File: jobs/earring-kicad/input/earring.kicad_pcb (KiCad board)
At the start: 4 copper layers, 30.5 x 35.8 mm, 144 parts, among them J1 USB-C, Q1 ALS-PT19, Q2 CJ2101, Q3 BSS138W, Q4 CJ2101, Q5 BSS138W, SW1 BOOTSEL, SW2 PWR, U1 RP2350A, U2 LGS4056H, U3 NCP730-3.3, U4 TPS22913, U5 USBLC6-2P6, U6 LSM6DS3TR-C, U7 W25Q16JVUXIQ, Y1 12MHz

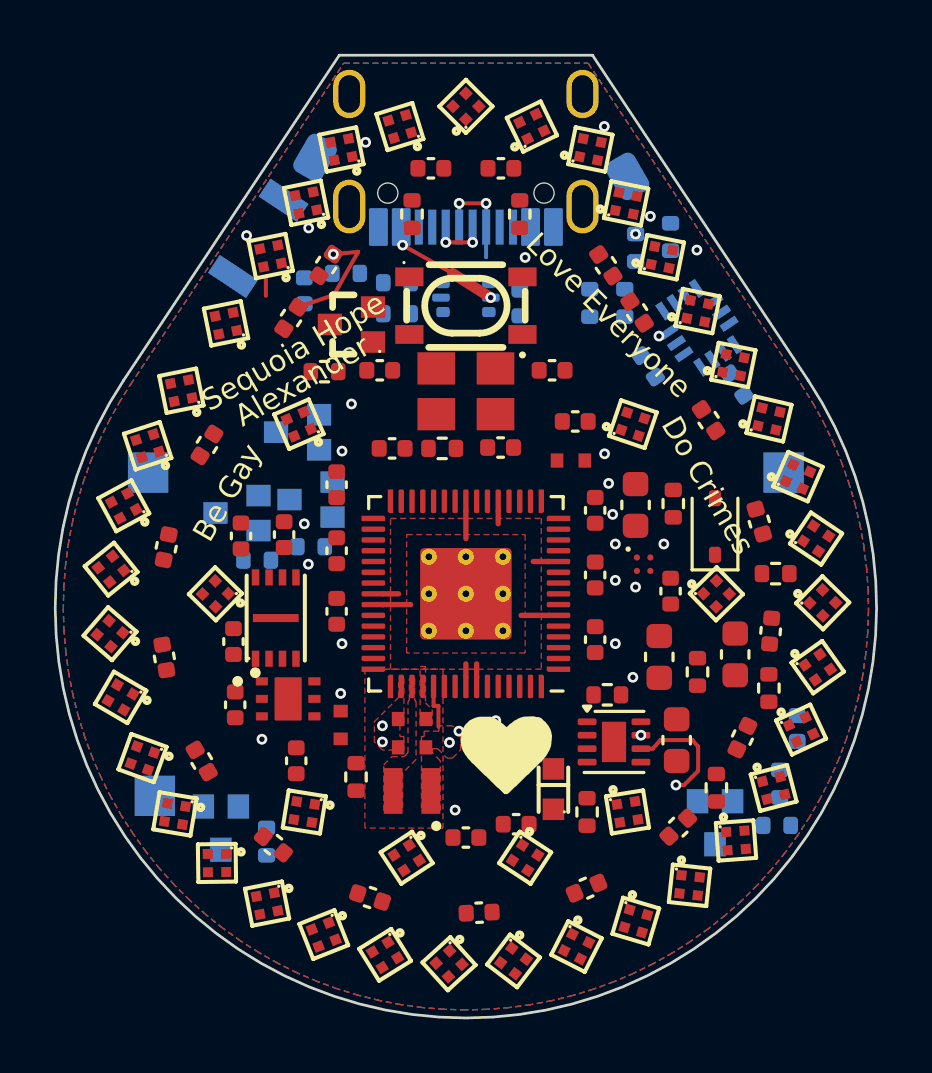
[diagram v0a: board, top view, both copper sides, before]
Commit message: Studio: KiCad colours and controls, views by side, router activity, fading congestion; the latest earring
The studio offers only the KiCad boards marked for it, bluebuzz and the earring, both from bare
pads (--strip-all), and the earring is now simple-earring's latest board (78920f1, the WS2816C
ring). It draws in KiCad's default colours with an active layer, high contrast and a flipped
view, takes KiCad's view keys, and shows all layers, the top, the bottom or both side by side.
The router reports what it is doing: a console streams its activity, the connection or part in
hand pulses on the board, and negotiation's threaded rounds show their trial routes as they come.
Congestion cells pop in when they change and fade while they stay. Old zone fills are hidden by
default, hovering a lock highlights its parts, and Route says what a run will do, with moving
parts a switch rather than a second button.

Co-Authored-By: Claude Opus 5.5 <noreply@anthropic.com>
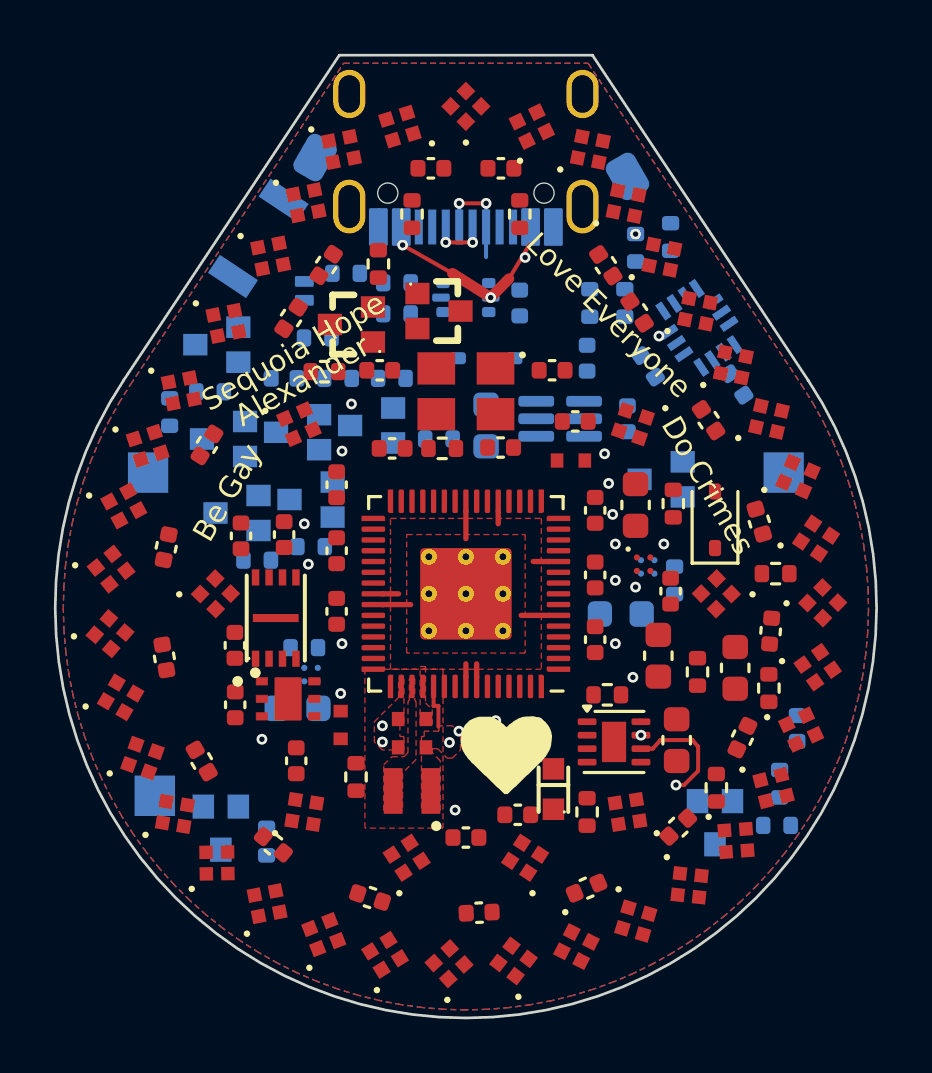
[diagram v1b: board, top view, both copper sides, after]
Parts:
- removed SW1: BOOTSEL, earring:KEY-SMD_4P-L4.2-W3.2-P2.20-LS4.6
- added C75: 10u, earring:C_0603_1608Metric, B.Cu at (100.8, 93.2)
- added C76: 10n, earring:C_0402_1005Metric, B.Cu at (104.5, 90.8)
- added C77: 100n, earring:C_0402_1005Metric, B.Cu at (106.0, 93.0)
- added C78: 10u, earring:C_0603_1608Metric, B.Cu at (105.8, 100.2)
- added C79: 10u, earring:C_0603_1608Metric, B.Cu at (93.8, 103.8)
- added D5: 1N4148WS, earring:D_SOD-323, B.Cu at (100.8, 90.8)
- added D6: PESD5V0S1BL, earring:D_SOD-882, B.Cu at (94.0, 88.2)
- added Q10: BSS138W, earring:SOT-323_MOSFET, B.Cu at (91.0, 93.8)
- added Q6: BSS138W, earring:SOT-323_MOSFET, F.Cu at (99.0, 89.0)
- added Q7: BSS138W, earring:SOT-323_MOSFET, B.Cu at (107.2, 95.2)
- added Q8: CJ2101, earring:SOT-323_MOSFET, B.Cu at (96.5, 93.2)
- added Q9: BSS138W, earring:SOT-323_MOSFET, B.Cu at (90.8, 90.2)
- added R26: 100k, earring:R_0402_1005Metric, B.Cu at (97.2, 91.5)
- added R27: 4.7k, earring:R_0402_1005Metric, B.Cu at (95.2, 91.5)
- added R28: 680k, earring:R_0402_1005Metric, B.Cu at (99.0, 93.8)
- added R29: 1M, earring:R_0402_1005Metric, F.Cu at (96.8, 87.2)
- added R30: 1k, earring:R_0402_1005Metric, B.Cu at (94.5, 90.0)
- added R31: 1k, earring:R_0402_1005Metric, B.Cu at (90.5, 92.0)
- added R32: 1k, earring:R_0402_1005Metric, B.Cu at (89.0, 92.8)
- added R33: 10k, earring:R_0402_1005Metric, B.Cu at (107.8, 99.0)
- added R34: 10k, earring:R_0402_1005Metric, B.Cu at (94.0, 101.5)
- added U10: TPS22913, earring:YZV0004ADAD, B.Cu at (94.2, 102.5)
- added U8: 74LVC2G14, earring:SOT-363_SC-70-6, B.Cu at (103.5, 93.0)
- added U9: TPS22913, earring:YZV0004ADAD, B.Cu at (106.8, 98.5)
- D2: value BAT54S -> BAV99W
- D3: value B5819WS -> 1N4007WS
- LED1, LED10, LED11, LED12, LED13, LED14, LED15, LED16, LED17, LED18, LED19, LED2, LED20, LED21, LED22, LED23, LED24, LED25, LED26, LED27, LED28, LED29, LED3, LED30, LED31, LED32, LED33, LED34, LED35, LED36, LED37, LED38, LED39, LED4, LED40, LED41, LED42, LED43, LED44, LED45, LED5, LED6, LED7, LED8, LED9: value SK6805-EC10 -> WS2816C-1313; footprint earring:LED_SK6805-EC10 -> earring:LED_WS2816C-1313
- Q4: value CJ2101 -> LBSS84WT1G
- moved C27 3.34 mm to (93.2, 91.5), turned to 0 degrees
- moved C29 0.50 mm to (110.0, 102.2)
- moved C26 0.36 mm to (101.9, 107.7)
- moved D3 0.25 mm to (109.2, 96.8)
- moved C18 0.15 mm to (91.4, 101.4)
- moved C17 0.06 mm to (107.1, 101.8)
- turned LED1 to 11.4366 degrees
- turned LED10 to 59.6219 degrees
- turned LED11 to 70.003 degrees
- turned LED12 to 80.3842 degrees
- turned LED13 to 90.7653 degrees
- turned LED14 to 101.146 degrees
- turned LED15 to 111.528 degrees
- turned LED16 to 121.909 degrees
- turned LED17 to 132.29 degrees
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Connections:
- net LED_D19 renamed LEDR_D18
- net LED_D20 renamed LEDR_D17
- net LED_D21 renamed LEDR_D16
- net LED_D22 renamed LEDR_D15
- net LED_D23 renamed LEDR_D14
- net LED_D24 renamed LEDR_D13
- net LED_D25 renamed LEDR_D12
- net LED_D26 renamed LEDR_D11
- net LED_D27 renamed LEDR_D10
- net LED_D28 renamed LEDR_D9
- net LED_D29 renamed LEDR_D8
- net LED_D30 renamed LEDR_D7
- net LED_D31 renamed LEDR_D6
- net LED_D32 renamed LEDR_D5
- net LED_D33 renamed LEDR_D4
- net LED_D34 renamed LEDR_D3
- net LED_D35 renamed LEDR_D2
- net LED_D36 renamed LEDR_D1
- net LED_DATA renamed LED_DATA_L
- net LED_EN renamed LED_EN_L
- C20 pad 1: VLED -> VLED_L
- C30 pad 1: VLED -> VLED_L
- C32 pad 1: VLED -> VLED_L
- C34 pad 1: VLED -> VLED_L
- C36 pad 1: VLED -> VLED_L
- C38 pad 1: VLED -> VLED_L
- C40 pad 1: VLED -> VLED_L
- C42 pad 1: VLED -> VLED_L
- C44 pad 1: VLED -> VLED_L
- C46 pad 1: VLED -> VLED_L
- C48 pad 1: VLED -> VLED_R
- C50 pad 1: VLED -> VLED_R
- C52 pad 1: VLED -> VLED_R
- C54 pad 1: VLED -> VLED_R
- C56 pad 1: VLED -> VLED_R
- C58 pad 1: VLED -> VLED_R
- C60 pad 1: VLED -> VLED_R
- C62 pad 1: VLED -> VLED_R
- C64 pad 1: VLED -> VLED_R
- C66 pad 1: VLED -> VLED_R
- C68 pad 1: VLED -> VLED_C
- C70 pad 1: VLED -> VLED_C
- C72 pad 1: VLED -> VLED_C
- C74 pad 1: VLED -> VLED_C
- D4 pad 1: BTN_SENSE -> PRESS_N
- LED1 pad 1: GND -> VLED_L
- LED1 pad 2: LED_D0 -> LEDL_D1
- LED1 pad 3: VLED -> GND
- LED1 pad 4: LED_D1 -> LEDL_D0
- LED10 pad 1: GND -> VLED_L
- LED10 pad 2: LED_D9 -> LEDL_D10
- LED10 pad 3: VLED -> GND
- LED10 pad 4: LED_D10 -> LEDL_D9
- LED11 pad 1: GND -> VLED_L
- LED11 pad 2: LED_D10 -> LEDL_D11
- LED11 pad 3: VLED -> GND
- LED11 pad 4: LED_D11 -> LEDL_D10
- LED12 pad 1: GND -> VLED_L
- LED12 pad 2: LED_D11 -> LEDL_D12
- LED12 pad 3: VLED -> GND
- LED12 pad 4: LED_D12 -> LEDL_D11
- LED13 pad 1: GND -> VLED_L
- LED13 pad 2: LED_D12 -> LEDL_D13
- LED13 pad 3: VLED -> GND
- LED13 pad 4: LED_D13 -> LEDL_D12
- LED14 pad 1: GND -> VLED_L
- LED14 pad 2: LED_D13 -> LEDL_D14
- LED14 pad 3: VLED -> GND
- LED14 pad 4: LED_D14 -> LEDL_D13
- LED15 pad 1: GND -> VLED_L
- LED15 pad 2: LED_D14 -> LEDL_D15
- LED15 pad 3: VLED -> GND
- LED15 pad 4: LED_D15 -> LEDL_D14
- LED16 pad 1: GND -> VLED_L
- LED16 pad 2: LED_D15 -> LEDL_D16
- LED16 pad 3: VLED -> GND
- LED16 pad 4: LED_D16 -> LEDL_D15
- LED17 pad 1: GND -> VLED_L
- LED17 pad 2: LED_D16 -> LEDL_D17
- LED17 pad 3: VLED -> GND
- LED17 pad 4: LED_D17 -> LEDL_D16
- LED18 pad 1: GND -> VLED_L
- LED18 pad 2: LED_D17 -> (no net)
- LED18 pad 3: VLED -> GND
- LED18 pad 4: LED_D18 -> LEDL_D17
- LED19 pad 1: GND -> VLED_R
- LED19 pad 2: LED_D18 -> (no net)
- LED19 pad 3: VLED -> GND
- LED2 pad 1: GND -> VLED_L
- LED2 pad 2: LED_D1 -> LEDL_D2
- LED2 pad 3: VLED -> GND
- LED2 pad 4: LED_D2 -> LEDL_D1
- LED20 pad 1: GND -> VLED_R
- LED20 pad 3: VLED -> GND
- LED21 pad 1: GND -> VLED_R
- LED21 pad 3: VLED -> GND
- LED22 pad 1: GND -> VLED_R
- LED22 pad 3: VLED -> GND
- LED23 pad 1: GND -> VLED_R
- LED23 pad 3: VLED -> GND
- LED24 pad 1: GND -> VLED_R
- LED24 pad 3: VLED -> GND
- LED25 pad 1: GND -> VLED_R
- LED25 pad 3: VLED -> GND
- LED26 pad 1: GND -> VLED_R
- LED26 pad 3: VLED -> GND
- LED27 pad 1: GND -> VLED_R
- LED27 pad 3: VLED -> GND
- LED28 pad 1: GND -> VLED_R
- LED28 pad 3: VLED -> GND
- LED29 pad 1: GND -> VLED_R
- LED29 pad 3: VLED -> GND
- LED3 pad 1: GND -> VLED_L
- LED3 pad 2: LED_D2 -> LEDL_D3
- LED3 pad 3: VLED -> GND
- LED3 pad 4: LED_D3 -> LEDL_D2
- LED30 pad 1: GND -> VLED_R
- LED30 pad 3: VLED -> GND
- LED31 pad 1: GND -> VLED_R
- LED31 pad 3: VLED -> GND
- LED32 pad 1: GND -> VLED_R
- LED32 pad 3: VLED -> GND
- LED33 pad 1: GND -> VLED_R
- LED33 pad 3: VLED -> GND
- LED34 pad 1: GND -> VLED_R
- LED34 pad 3: VLED -> GND
- LED35 pad 1: GND -> VLED_R
- LED35 pad 3: VLED -> GND
- LED36 pad 1: GND -> VLED_R
- LED36 pad 3: VLED -> GND
- LED37 pad 1: GND -> VLED_R
- LED37 pad 3: VLED -> GND
- LED37 pad 4: LED_D37 -> LEDR_D0
- LED38 pad 1: GND -> VLED_C
- LED38 pad 2: LED_D37 -> LEDC_D1
- LED38 pad 3: VLED -> GND
- LED38 pad 4: LED_D38 -> LEDC_D0
- LED39 pad 1: GND -> VLED_C
- LED39 pad 2: LED_D38 -> LEDC_D2
- LED39 pad 3: VLED -> GND
- LED39 pad 4: LED_D39 -> LEDC_D1
- LED4 pad 1: GND -> VLED_L
- LED4 pad 2: LED_D3 -> LEDL_D4
- LED4 pad 3: VLED -> GND
- LED4 pad 4: LED_D4 -> LEDL_D3
- LED40 pad 1: GND -> VLED_C
- LED40 pad 2: LED_D39 -> LEDC_D3
- LED40 pad 3: VLED -> GND
- LED40 pad 4: LED_D40 -> LEDC_D2
- LED41 pad 1: GND -> VLED_C
- LED41 pad 2: LED_D40 -> LEDC_D4
- LED41 pad 3: VLED -> GND
- LED41 pad 4: LED_D41 -> LEDC_D3
- LED42 pad 1: GND -> VLED_C
- LED42 pad 2: LED_D41 -> LEDC_D5
- LED42 pad 3: VLED -> GND
- LED42 pad 4: LED_D42 -> LEDC_D4
- LED43 pad 1: GND -> VLED_C
- LED43 pad 2: LED_D42 -> LEDC_D6
- LED43 pad 3: VLED -> GND
- LED43 pad 4: LED_D43 -> LEDC_D5
- LED44 pad 1: GND -> VLED_C
- LED44 pad 2: LED_D43 -> LEDC_D7
- LED44 pad 3: VLED -> GND
- LED44 pad 4: LED_D44 -> LEDC_D6
- LED45 pad 1: GND -> VLED_C
- LED45 pad 2: LED_D44 -> (no net)
- LED45 pad 3: VLED -> GND
- LED45 pad 4: (no net) -> LEDC_D7
- LED5 pad 1: GND -> VLED_L
- LED5 pad 2: LED_D4 -> LEDL_D5
- LED5 pad 3: VLED -> GND
- LED5 pad 4: LED_D5 -> LEDL_D4
- LED6 pad 1: GND -> VLED_L
- LED6 pad 2: LED_D5 -> LEDL_D6
- LED6 pad 3: VLED -> GND
- LED6 pad 4: LED_D6 -> LEDL_D5
- LED7 pad 1: GND -> VLED_L
- LED7 pad 2: LED_D6 -> LEDL_D7
- LED7 pad 3: VLED -> GND
- LED7 pad 4: LED_D7 -> LEDL_D6
- LED8 pad 1: GND -> VLED_L
- LED8 pad 2: LED_D7 -> LEDL_D8
- LED8 pad 3: VLED -> GND
- LED8 pad 4: LED_D8 -> LEDL_D7
- LED9 pad 1: GND -> VLED_L
- LED9 pad 2: LED_D8 -> LEDL_D9
- LED9 pad 3: VLED -> GND
- LED9 pad 4: LED_D9 -> LEDL_D8
- Q3 pad 3: LED_D0 -> LEDL_D0
- R23 pad 1: VLED -> VLED_L
- R23 pad 2: LED_D0 -> LEDL_D0
- SW2 pad 2: BTN_N -> BTN_EXT
- U1 pad 2: (no net) -> LED_EN_R
- U1 pad 27: (no net) -> LED_DATA_C
- U1 pad 28: (no net) -> LED_DATA_R
- U1 pad 34: (no net) -> LED_EN_C
- U4 pad A1: VLED -> VLED_L
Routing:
- net VLED: track 4.17 -> 0.00 mm, vias 7 -> 0
- net VBUS: track 3.81 -> 6.24 mm
- net LED_D3: track 0.62 -> 0.00 mm
- added copper zone on In2.Cu, net VLED_C
- added copper zone on In2.Cu, net VLED_L
- added copper zone on In2.Cu, net VLED_R
- removed copper zone on In2.Cu, net VLED
